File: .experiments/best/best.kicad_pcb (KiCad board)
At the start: 2 copper layers, 90 x 58 mm, 39 parts, among them J1 USB_C, J2 Output, J3 Debug, Q1 FS8205A, U1 USBLC6-2SC6, U2 BQ24072, U3 HY2113-KB5B, U4 MT3608, U5 AP2112K-3.3, U6 LN61CN3302MR-G

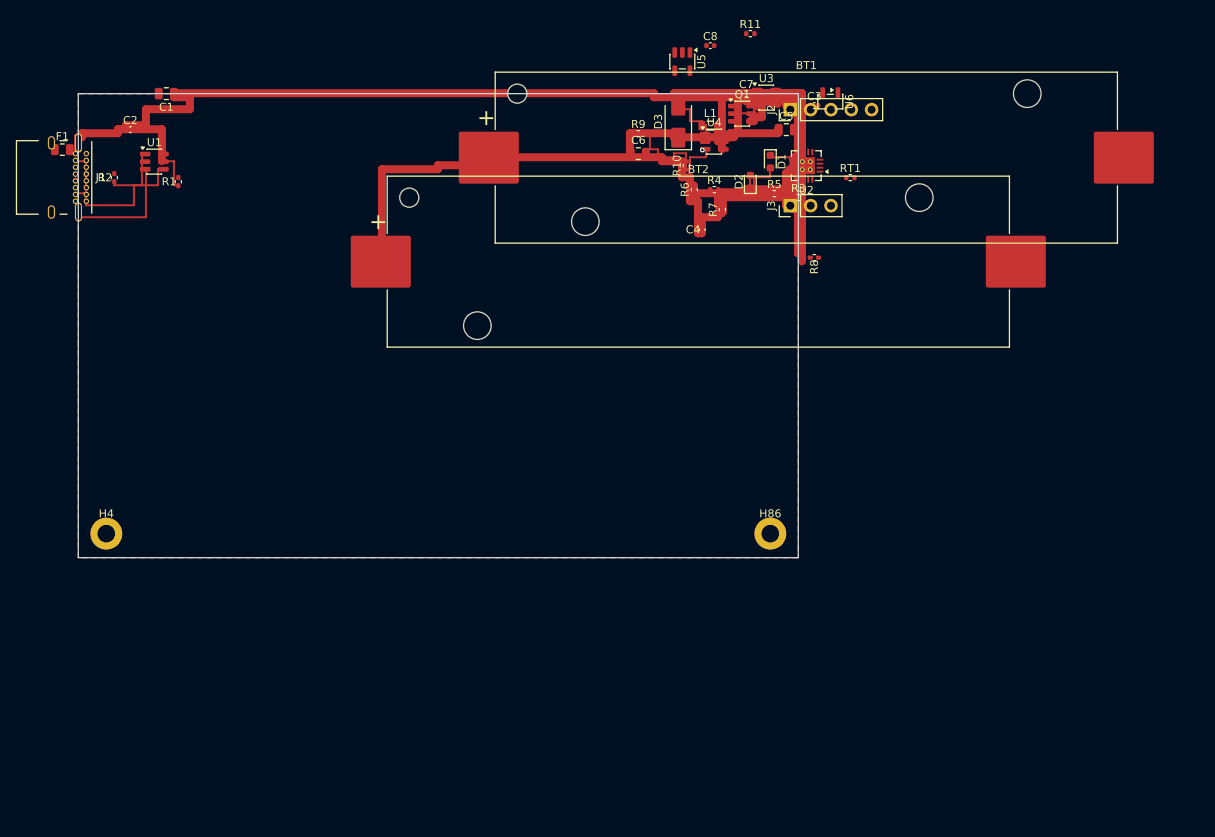
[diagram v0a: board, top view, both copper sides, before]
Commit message: 300 experiments: best 79.3, 27/27 routed, 2 vias, 880mm traces
First run with courtyard overlap scoring, intra-cluster optimization,
and reduced compactness penalty. 15/300 kept improvements.

Co-Authored-By: Claude Opus 4.6 <noreply@anthropic.com>
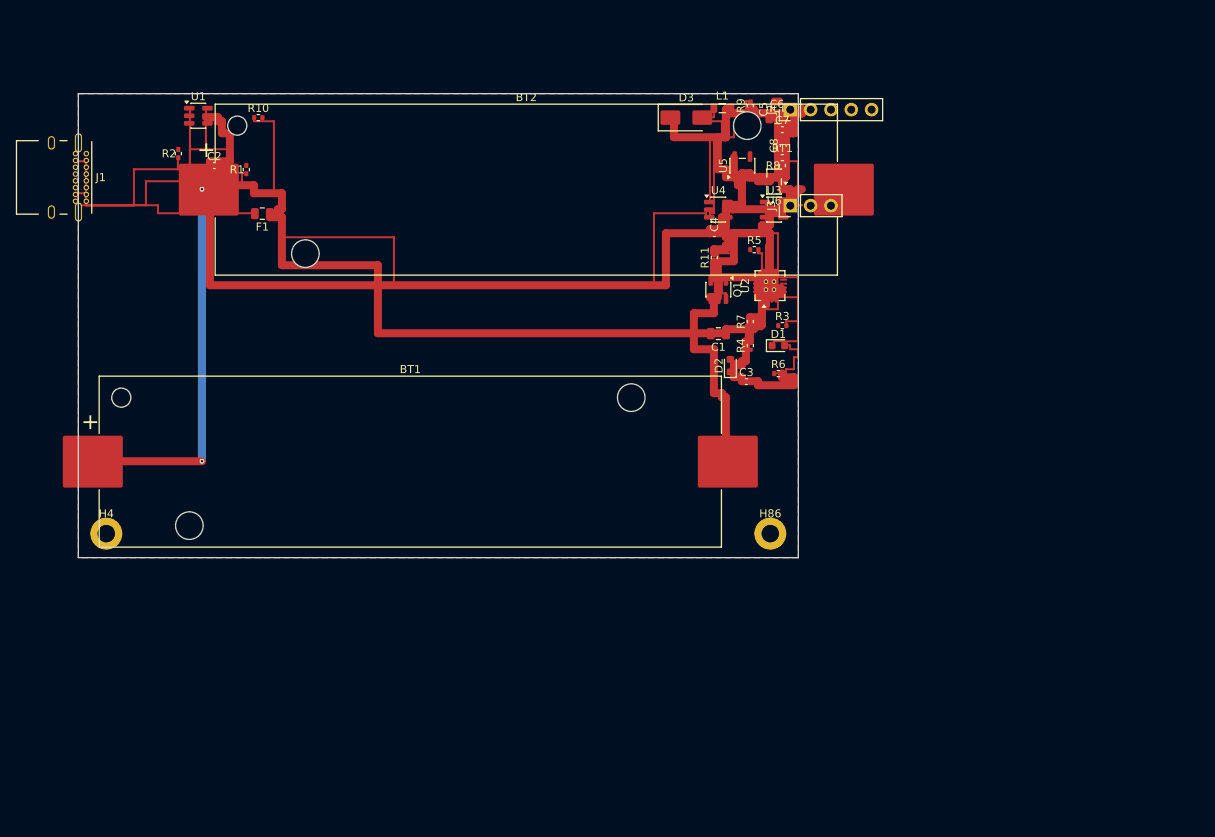
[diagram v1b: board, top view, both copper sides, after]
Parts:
- moved C1 75.2 mm to (80.0, 30.0)
- moved BT1 62.4 mm to (41.5, 46.0)
- moved R10 53.8 mm to (22.5, 3.00), turned to 0 degrees
- moved C3 35.5 mm to (83.5, 36.0)
- moved R11 28.4 mm to (79.5, 20.5), turned to 90 degrees
- moved F1 26.2 mm to (23.0, 15.0), turned to 180 degrees
- moved R6 25.3 mm to (87.5, 35.0), turned to 0 degrees
- moved BT2 23.3 mm to (56.0, 12.0)
- moved D2 23.1 mm to (81.5, 34.0)
- moved D1 23.0 mm to (87.5, 31.5), turned to 0 degrees
- moved Q1 22.2 mm to (80.0, 24.5), turned to -90 degrees
- moved R4 20.0 mm to (84.0, 31.5), turned to 90 degrees
- moved C6 17.9 mm to (87.3, 3.00)
- moved R3 16.1 mm to (88.0, 29.0)
- moved U2 15.7 mm to (86.5, 24.0), turned to 90 degrees
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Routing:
- net Net-(U4-FB): track 16.0 -> 107.0 mm
- net /VBAT: track 108.5 -> 174.5 mm, vias 0 -> 2
- net Net-(F1-Pad2): track 7.50 -> 29.5 mm
- net /CHG_N: track 10.0 -> 28.0 mm
- net /VSYS_BOOST: track 11.0 -> 26.0 mm
- net /NTC_SENSE: track 11.0 -> 26.0 mm
- net Net-(Q1B-G): track 2.00 -> 16.0 mm
- net Net-(J1-CC1): track 19.0 -> 30.0 mm
- net Net-(R1-Pad1): track 6.00 -> 16.0 mm
- net Net-(D3-A): track 7.00 -> 17.0 mm
- net /VBUS: track 120.5 -> 111.5 mm
- net Net-(Q1A-G): track 7.50 -> 16.0 mm
- net /CELL_NEG: track 44.0 -> 52.5 mm
- net Net-(U2-ISET): track 2.50 -> 10.5 mm
- net Net-(J1-CC2): track 18.0 -> 26.0 mm
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
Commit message: Add scoring breakdown + DRC panels to dashboard, 100 experiments
Dashboard now has 4 panels:
1. Score per round with best-so-far line
2. Category score breakdown (placement, route completion, trace
   efficiency, via score, courtyard overlap, containment)
3. DRC violations stacked bar (shorts, unconnected, clearance, courtyard)
4. Config heatmap for kept experiments

Each experiment now logs per-category scores and DRC counts to JSONL.
Best: 78.7, 27/27 routed, 4 vias, 830mm traces.

Co-Authored-By: Claude Opus 4.6 <noreply@anthropic.com>
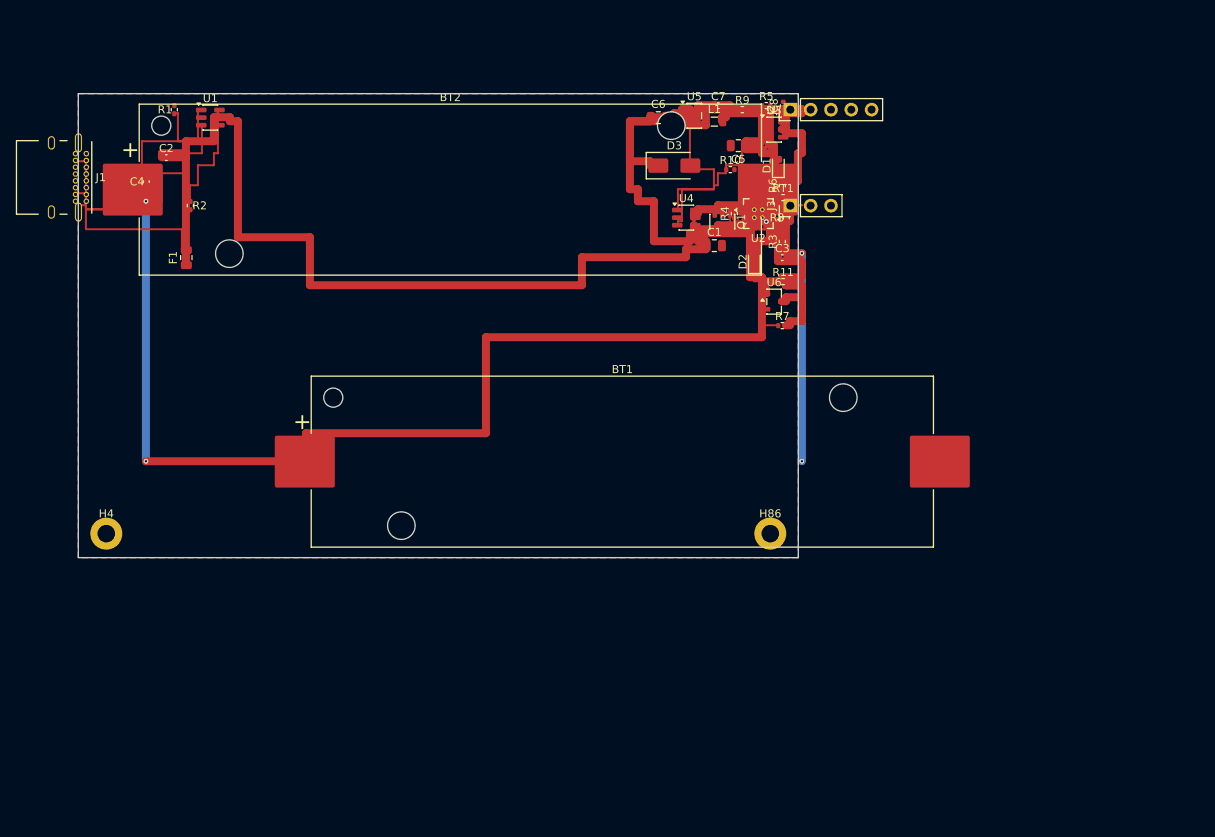
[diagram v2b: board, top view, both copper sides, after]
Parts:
- moved C4 71.3 mm to (8.50, 11.0), turned to 90 degrees
- moved R10 59.4 mm to (81.5, 9.50)
- moved BT1 26.5 mm to (68.0, 46.0)
- moved R6 23.5 mm to (88.0, 11.5), turned to 90 degrees
- moved D1 22.5 mm to (87.5, 9.00), turned to 90 degrees
- moved R5 18.1 mm to (86.0, 1.50)
- moved R4 16.6 mm to (82.0, 15.0)
- moved C3 16.1 mm to (88.0, 20.5)
- moved U6 15.0 mm to (87.0, 26.0), turned to 0 degrees
- moved C6 14.8 mm to (72.5, 3.00)
- moved D2 13.3 mm to (84.5, 21.0)
- moved R1 11.7 mm to (12.0, 2.00)
- moved C1 11.0 mm to (79.5, 19.0), turned to 0 degrees
- moved F1 11.0 mm to (13.5, 20.5), turned to 90 degrees
- moved R3 10.5 mm to (88.0, 18.5), turned to 90 degrees
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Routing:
- net Net-(U4-FB): track 107.0 -> 27.0 mm
- net /EN: track 32.0 -> 74.5 mm
- net /NTC_SENSE: track 26.0 -> 9.00 mm
- net /VBUS: track 111.5 -> 126.0 mm
- net /CHG_N: track 28.0 -> 15.5 mm
- net Net-(U2-TMR): track 5.50 -> 17.5 mm
- net /CELL_NEG: track 52.5 -> 64.5 mm, vias 0 -> 2
- net Net-(D2-K): track 17.5 -> 9.00 mm
- net /VSYS_BOOST: track 26.0 -> 34.5 mm
- net Net-(U2-ILIM): track 10.5 -> 3.00 mm
- net Net-(U2-ISET): track 10.5 -> 3.50 mm
- net /3V3: track 19.5 -> 12.5 mm
- net Net-(D2-A): track 7.00 -> 11.5 mm
- net Net-(D1-A): track 8.00 -> 4.00 mm
- net Net-(F1-Pad2): track 29.5 -> 25.5 mm
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
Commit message: 100-round experiment: log-scale shorts penalty + baseline parity
Add logarithmic shorts penalty so DRC failures still produce a gradient
for the optimizer to descend, and apply the same penalty to the baseline
so kept improvements are directly comparable. 13/100 rounds kept.

Co-Authored-By: Claude Opus 4.6 <noreply@anthropic.com>
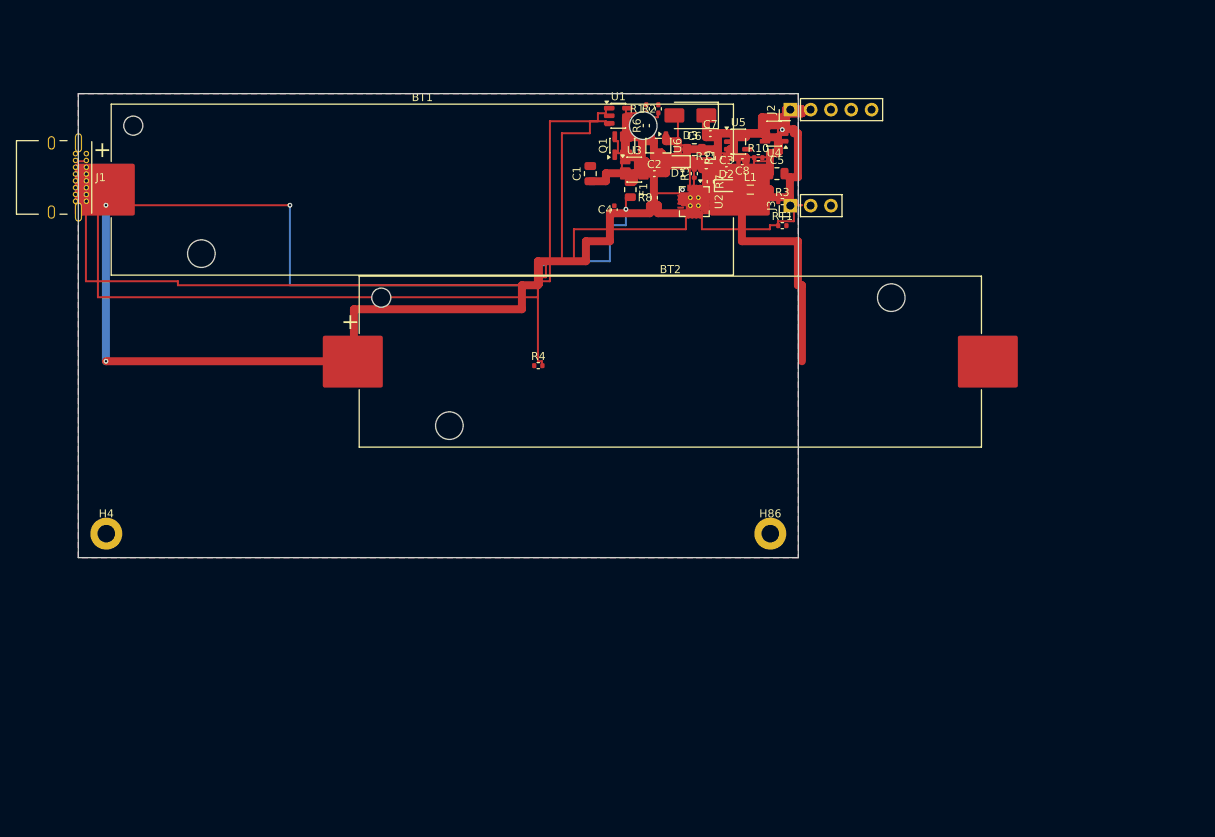
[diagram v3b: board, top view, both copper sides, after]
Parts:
- moved C2 61.0 mm to (72.0, 10.0)
- moved R2 59.7 mm to (72.5, 1.90), turned to 90 degrees
- moved R1 59.0 mm to (71.0, 1.90)
- moved C4 58.6 mm to (67.0, 14.5)
- moved F1 56.1 mm to (69.0, 12.0), turned to -90 degrees
- moved U1 51.0 mm to (67.5, 2.76)
- moved BT1 42.2 mm to (43.0, 12.0)
- moved BT2 34.9 mm to (74.0, 33.5)
- moved R4 31.0 mm to (57.5, 34.0), turned to 0 degrees
- moved U6 24.3 mm to (72.5, 6.50), turned to -90 degrees
- moved R7 20.1 mm to (79.0, 11.0), turned to -90 degrees
- moved R6 18.6 mm to (71.0, 4.00)
- moved U3 18.2 mm to (69.5, 9.50)
- moved C1 17.9 mm to (64.0, 10.0), turned to 90 degrees
- moved R11 17.4 mm to (78.5, 9.00)
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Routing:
- net /VBUS: track 126.0 -> 34.0 mm
- net Net-(J1-CC2): track 28.5 -> 102.5 mm
- net Net-(F1-Pad2): track 25.5 -> 97.5 mm, vias 0 -> 2
- net Net-(J1-CC1): track 32.5 -> 102.5 mm
- net /EN: track 74.5 -> 26.5 mm
- net Net-(U2-ILIM): track 3.00 -> 40.0 mm
- net /VSYS_BOOST: track 34.5 -> 11.0 mm
- net /NTC_SENSE: track 9.00 -> 27.0 mm
- net Net-(Q1A-G): track 19.0 -> 1.50 mm
- net Net-(U4-FB): track 27.0 -> 12.5 mm
- net Net-(Q1B-G): track 19.0 -> 5.50 mm
- net Net-(U2-TMR): track 17.5 -> 6.00 mm
- net /CHG_N: track 15.5 -> 26.0 mm
- net Net-(R1-Pad1): track 13.0 -> 3.00 mm
- net /CELL_NEG: track 64.5 -> 54.5 mm, vias 2 -> 0
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
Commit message: 30-round parallel experiment: 26/26 nets routed, score 2.72
- 30 rounds with 10 parallel workers completed in ~2m40s wall time
- Best result: score=2.72, 26/26 nets routed (0 failed), 56 vias
- Best config: clearance=0.193mm, force_attract_k=0.019,
  cooling_factor=0.975, existing_trace_cost=200
- Updated experiments.jsonl (42 total entries), dashboard PNG

Co-Authored-By: Claude Sonnet 4.6 <noreply@anthropic.com>
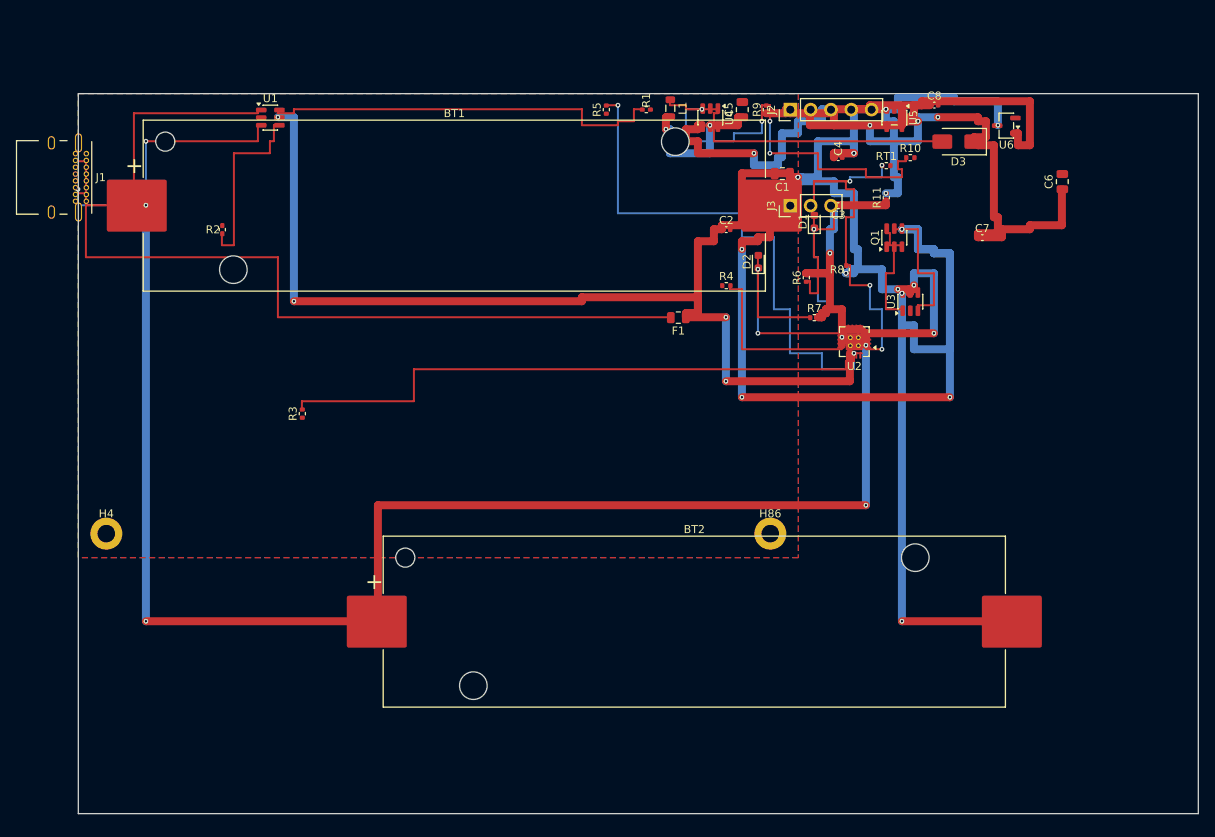
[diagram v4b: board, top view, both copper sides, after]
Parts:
- moved R3 65.6 mm to (28.0, 40.0), turned to 90 degrees
- moved R2 56.6 mm to (18.0, 17.0)
- moved C6 46.2 mm to (123.0, 11.0), turned to 90 degrees
- moved U6 43.6 mm to (116.0, 4.00), turned to 180 degrees
- moved U1 43.5 mm to (24.0, 3.00)
- moved U3 38.2 mm to (104.0, 26.0), turned to 90 degrees
- moved C7 36.4 mm to (113.0, 18.0)
- moved Q1 35.9 mm to (102.0, 18.0)
- moved D3 33.7 mm to (110.0, 6.00)
- moved BT2 32.6 mm to (77.0, 66.0)
- moved C4 28.7 mm to (95.0, 8.00), turned to 0 degrees
- moved R6 27.6 mm to (91.0, 23.0)
- moved U2 26.6 mm to (97.0, 31.0), turned to 180 degrees
- moved R8 25.6 mm to (96.0, 22.0)
- moved R4 25.5 mm to (81.0, 24.0)
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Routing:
- net /VBAT: track 165.5 -> 298.5 mm, vias 2 -> 14
- net /CELL_NEG: track 54.5 -> 169.0 mm, vias 0 -> 8
- net /VBUS: track 34.0 -> 143.0 mm, vias 0 -> 4
- net Net-(J1-CC2): track 102.5 -> 35.0 mm, vias 0 -> 2
- net Net-(U2-ISET): track 12.5 -> 77.0 mm
- net Net-(J1-CC1): track 102.5 -> 39.0 mm
- net Net-(U2-TMR): track 6.00 -> 66.0 mm, vias 0 -> 2
- net /5V: track 28.0 -> 80.5 mm, vias 1 -> 4
- net Net-(R1-Pad1): track 3.00 -> 50.5 mm
- net /EN: track 26.5 -> 71.5 mm, vias 0 -> 6
- net Net-(U4-FB): track 12.5 -> 50.5 mm, vias 0 -> 4
- net /NTC_SENSE: track 27.0 -> 51.0 mm, vias 0 -> 4
- net Net-(U2-ILIM): track 40.0 -> 22.0 mm
- net Net-(R2-Pad1): track 5.50 -> 23.5 mm
- net /VSYS: track 28.0 -> 41.5 mm, vias 0 -> 2
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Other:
- board size 90 x 58 mm -> 140 x 90 mm

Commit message: 25-round experiment: best score 2.52, dashboard updated, GIF dropped (no-render run)
Co-Authored-By: Claude Sonnet 4.6 <noreply@anthropic.com>
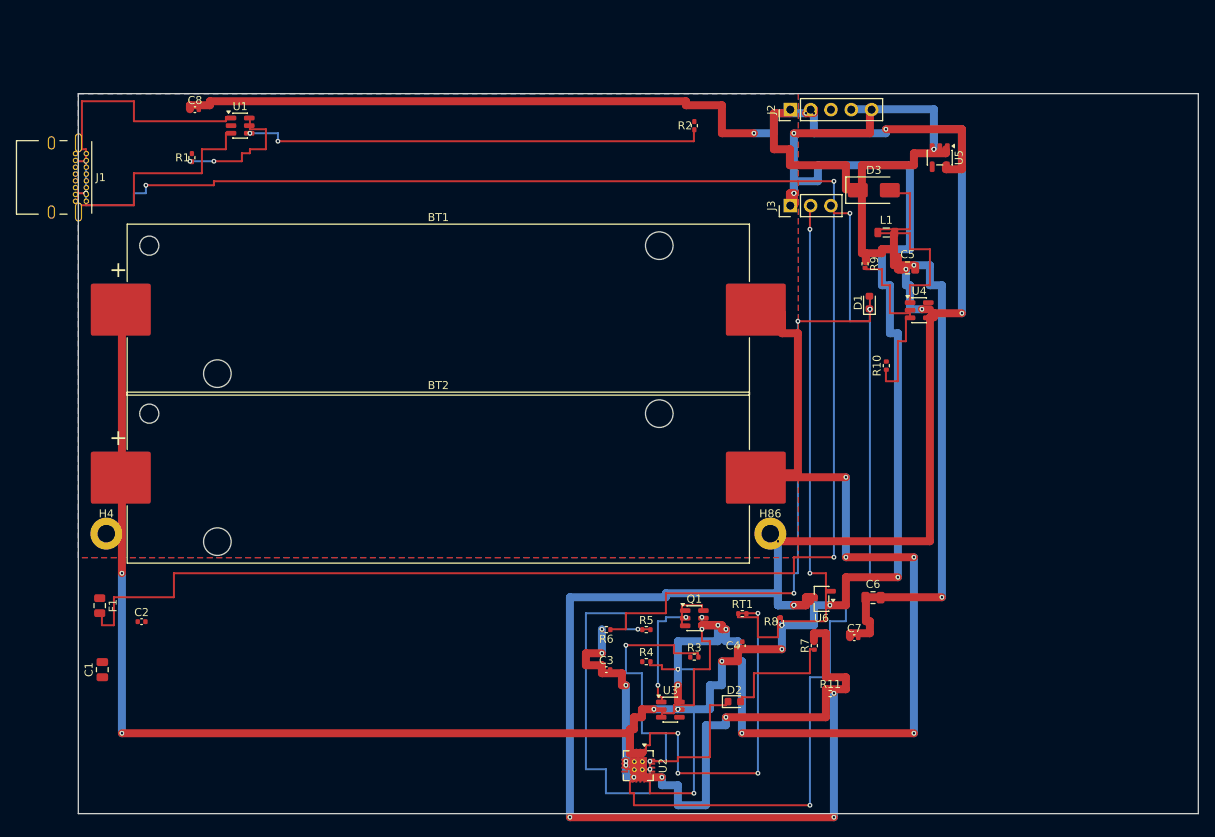
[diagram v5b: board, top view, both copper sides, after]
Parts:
- moved C1 105.2 mm to (3.00, 72.0), turned to 90 degrees
- moved C8 92.4 mm to (14.6, 2.00)
- moved C2 88.0 mm to (7.90, 66.0)
- moved F1 80.8 mm to (2.67, 64.0), turned to -90 degrees
- moved R5 65.2 mm to (71.0, 67.0), turned to 0 degrees
- moved C3 64.8 mm to (66.0, 72.0), turned to 0 degrees
- moved U6 63.5 mm to (92.9, 63.2)
- moved R11 62.4 mm to (94.0, 75.0), turned to 0 degrees
- moved C4 62.2 mm to (83.0, 69.0), turned to 90 degrees
- moved R2 60.4 mm to (77.0, 4.00)
- moved U2 59.5 mm to (70.0, 84.0), turned to -90 degrees
- moved U3 59.2 mm to (74.0, 77.0), turned to 0 degrees
- moved RT1 58.8 mm to (83.0, 65.0)
- moved R3 57.7 mm to (77.0, 70.4), turned to 0 degrees
- moved C6 57.1 mm to (99.3, 63.0), turned to 0 degrees
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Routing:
- net Net-(F1-Pad2): track 94.5 -> 253.0 mm, vias 0 -> 6
- net /EN: track 71.5 -> 219.0 mm, vias 6 -> 10
- net /VBUS: track 143.0 -> 0.00 mm, vias 4 -> 0
- net /3V3: track 19.5 -> 115.5 mm, vias 0 -> 4
- net /CHG_N: track 23.0 -> 117.0 mm, vias 2 -> 4
- net /NTC_SENSE: track 51.0 -> 115.0 mm, vias 4 -> 6
- net Net-(D1-A): track 13.0 -> 74.0 mm, vias 0 -> 2
- net Net-(U2-ISET): track 77.0 -> 32.0 mm, vias 0 -> 2
- net /VSYS: track 41.5 -> 83.0 mm, vias 2 -> 8
- net /5V: track 80.5 -> 120.5 mm, vias 4 -> 2
- net Net-(R2-Pad1): track 23.5 -> 58.0 mm, vias 0 -> 2
- net Net-(R1-Pad1): track 50.5 -> 17.0 mm, vias 0 -> 2
- net /CELL_NEG: track 169.0 -> 140.5 mm
- net Net-(U4-FB): track 50.5 -> 24.0 mm, vias 4 -> 0
- net Net-(U2-TMR): track 66.0 -> 43.5 mm
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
